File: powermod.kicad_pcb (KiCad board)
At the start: 4 copper layers, 27 x 18 mm, 17 parts, among them J1 Conn_02x07_Odd_Even, J2 Conn_02x07_Odd_Even, U1 TPS54202

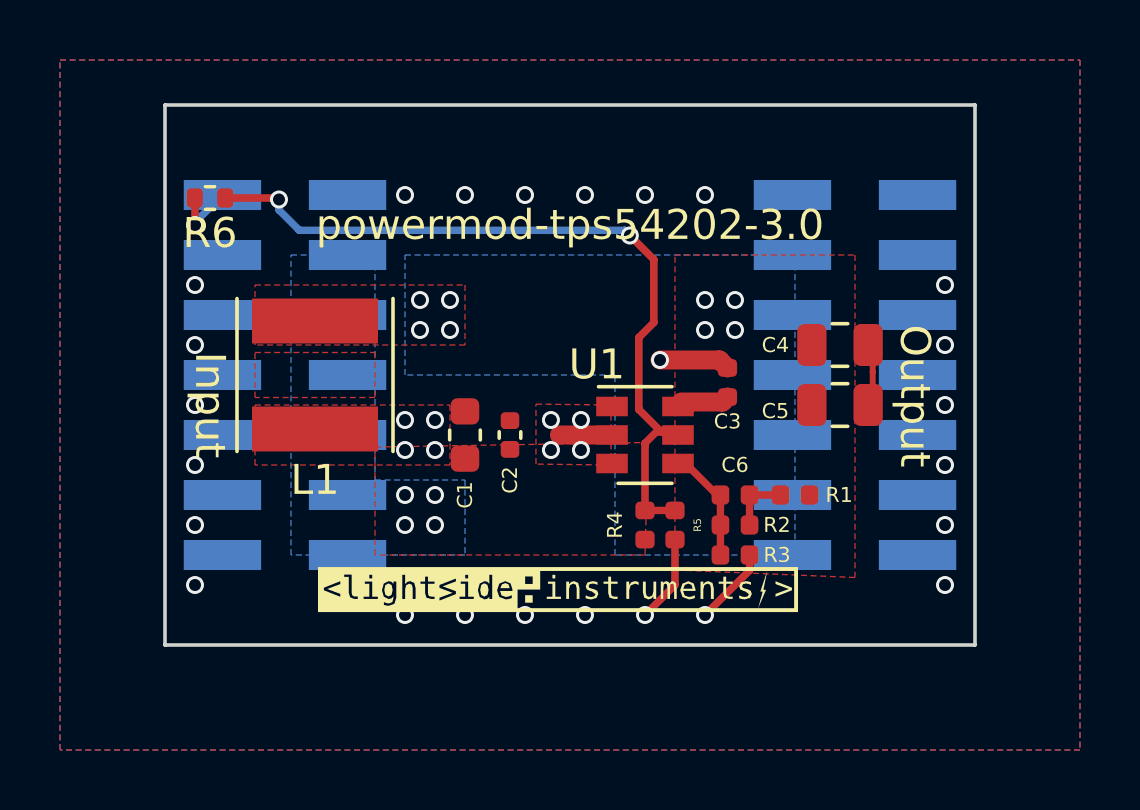
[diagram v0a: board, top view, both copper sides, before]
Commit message: powermod-tps54260
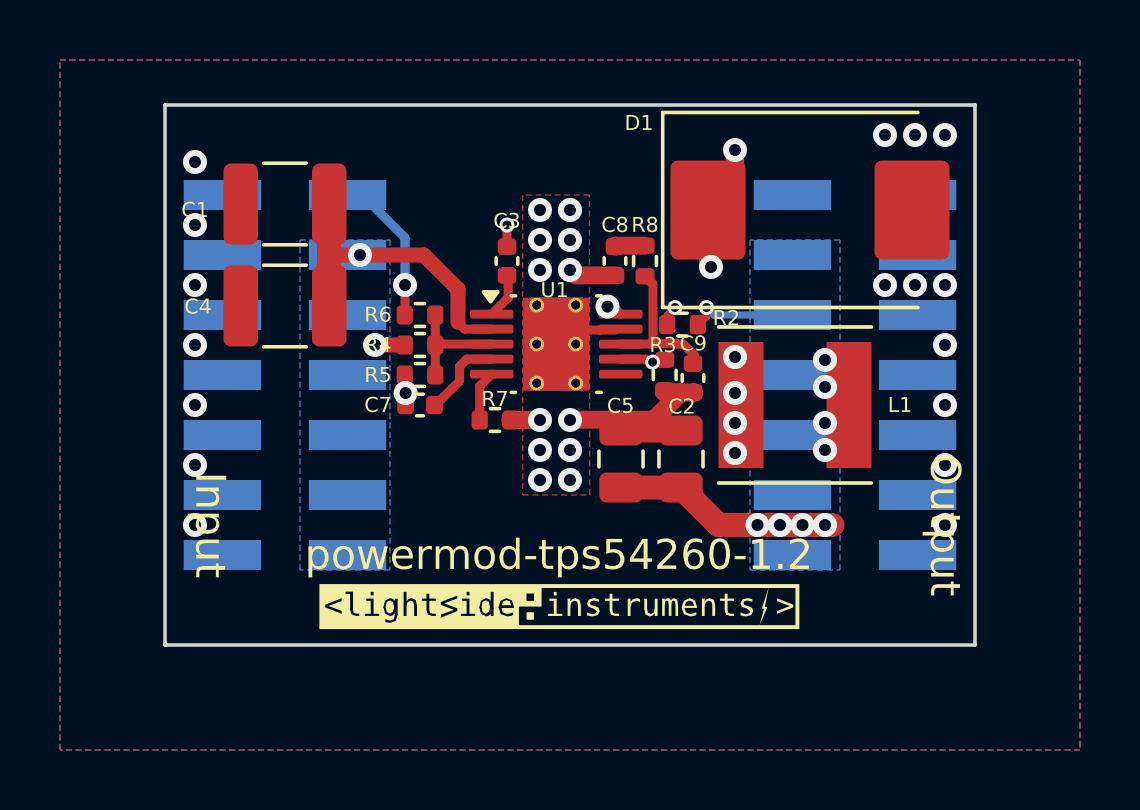
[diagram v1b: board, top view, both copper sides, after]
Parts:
- removed C6: 75 pF, Capacitor_SMD:C_0402_1005Metric
- removed R1: 49.9, Resistor_SMD:R_0402_1005Metric
- added C7: 0.025uF, Capacitor_SMD:C_0402_1005Metric, F.Cu at (24.5, 49.0)
- added C8: 51.1nF, Capacitor_SMD:C_0402_1005Metric, F.Cu at (31.0, 44.2)
- added C9: 14pF, Capacitor_SMD:C_0402_1005Metric, F.Cu at (33.6, 48.1)
- added D1: B360, Diode_SMD:D_SMC, F.Cu at (37.5, 42.5)
- added R7: 240K, Resistor_SMD:R_0402_1005Metric, F.Cu at (27.0, 49.5)
- added R8: 9K, Resistor_SMD:R_0402_1005Metric, F.Cu at (32.0, 44.2)
- C1: value 10uF -> 4.7uF; footprint Capacitor_SMD:C_0603_1608Metric -> Capacitor_SMD:C_1210_3225Metric
- C2: value 0.1uF -> 47uF; footprint Capacitor_SMD:C_0402_1005Metric -> Capacitor_SMD:C_0805_2012Metric
- C4: value 22uF -> 4.7uF; footprint Capacitor_SMD:C_0805_2012Metric -> Capacitor_SMD:C_1210_3225Metric
- C5: value 22uF -> 47uF
- R2: value 100K -> 52K
- R3: value 13.3K -> 11K
- R4: value 511K -> 332K
- R5: value 105K -> 56.2K
- U1: value TPS54202 -> TPS54260DGQ; footprint Package_TO_SOT_SMD:SOT-23-6 -> Package_SO:MSOP-10-1EP_3x3mm_P0.5mm_EP2.2x3.1mm_Mask1.83x1.89mm_ThermalVias
- moved C4 18.5 mm to (20.0, 45.7), turned to 180 degrees
- moved L1 16.0 mm to (37.0, 49.0), turned to 0 degrees
- moved R5 9.86 mm to (24.5, 48.0), turned to 0 degrees
- moved C1 9.76 mm to (20.0, 42.3), turned to 180 degrees
- moved R4 9.60 mm to (24.5, 47.0), turned to 0 degrees
- moved C3 8.39 mm to (27.4, 44.2)
- moved R6 8.01 mm to (24.5, 46.0)
- moved C5 7.52 mm to (31.2, 50.8), turned to 90 degrees
- moved R2 6.91 mm to (33.2, 46.3)
- moved R3 6.44 mm to (32.7, 48.0), turned to -90 degrees
- moved C2 5.76 mm to (33.2, 50.8)
- moved U1 4.24 mm to (29.0, 47.0)
- moved svg2mod 0.57 mm to (29.1, 56.3)
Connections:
- C2 pad 1: SYS_DCIN -> +5V
- C3 pad 2: Net-(C3-Pad2) -> /BOOT
- C4 pad 1: +5V -> SYS_DCIN
- J1 pad 1: unconnected-(J1-Pad1) -> Net-(J1-Pin_1)
- J1 pad 2: Net-(J1-Pad2) -> unconnected-(J1-Pin_2-Pad2)
- R2 pad 1: Net-(C6-Pad1) -> +5V
- R2 pad 2: Net-(C6-Pad2) -> /FB
- R3 pad 1: Net-(C6-Pad2) -> /FB
- R5 pad 1: /ENABLE -> GND
- R5 pad 2: GND -> /ENABLE
- R6 pad 2: Net-(J1-Pad2) -> Net-(J1-Pin_1)
- U1 pad 1: GND -> /BOOT
- U1 pad 2: /SW -> SYS_DCIN
- U1 pad 3: SYS_DCIN -> /ENABLE
- U1 pad 4: Net-(C6-Pad2) -> Net-(U1-SS/TR)
- U1 pad 5: /ENABLE -> Net-(U1-RT/CLK)
- U1 pad 6: Net-(C3-Pad2) -> unconnected-(U1-PWRGD-Pad6)
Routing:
- net /ENABLE: track 27.0 -> 3.91 mm, vias 2 -> 0
- net /SW: track 8.77 -> 22.4 mm, vias 9 -> 8
- net +5V: track 0.00 -> 11.5 mm, vias 8 -> 9
- net SYS_DCIN: track 0.00 -> 11.4 mm, vias 4 -> 2
- net Net-(U1-COMP): track 0.00 -> 5.22 mm
- net Net-(J1-Pin_1): track 0.00 -> 4.60 mm, vias 0 -> 1
- net /FB: track 0.00 -> 3.91 mm, vias 0 -> 2
- net Net-(C6-Pad2): track 3.74 -> 0.00 mm
- net GND: track 7.54 -> 11.2 mm, vias 24 -> 30
- net Net-(U1-SS/TR): track 0.00 -> 2.83 mm
- net Net-(J1-Pad2): track 2.28 -> 0.00 mm, vias 1 -> 0
- net Net-(C6-Pad1): track 2.03 -> 0.00 mm
- net Net-(U1-RT/CLK): track 0.00 -> 1.70 mm
- net Net-(C3-Pad2): track 1.63 -> 0.00 mm
- net /BOOT: track 0.00 -> 1.49 mm
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- added copper zone on In1.Cu, net /SW
- added copper zone on In2.Cu, net GND
- removed copper zone on F.Cu, net (none)
- removed copper zone on F.Cu, net +5V
- removed copper zone on F.Cu, net /SW
- removed copper zone on In2.Cu, net /SW
- removed copper zone on F.Cu, net SYS_DCIN
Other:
- board text added: "Enable pin"
- board text added: "powermod-tps54260-1.2"
- board text removed: "powermod-tps54202-3.0"

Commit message: powermod-tps54260-1.4
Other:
- board text added: "powermod-tps54260-1.4"
- board text removed: "powermod-tps54260-1.2"
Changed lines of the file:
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@@
 		)
 	)
-	(gr_text "powermod-tps54260-1.2"
+	(gr_text "powermod-tps54260-1.4"
 		(at 29.129989 54 0)
 		(layer "F.SilkS")
@@
 	)
 	(segment
+		(start 32.160854 46.838589)
+		(end 32.26686 46.944595)
+		(width 0.2)
+		(layer "F.Cu")
+		(net 14)
+	)
+	(segment
 		(start 33.28 46.97)
 		(end 33.071533 46.97)
@@
 	)
 	(segment
-		(start 32.265 44.975)
-		(end 32.265 46.87186)
-		(width 0.3)
+		(start 32.160854 45.079146)
+		(end 32.160854 46.838589)
+		(width 0.2)
 		(layer "F.Cu")
 		(net 14)
@@
 	)
 	(segment
-		(start 32.265 46.87186)
-		(end 32.229562 46.907298)
-		(width 0.3)
-		(layer "F.Cu")
-		(net 14)
-	)
-	(segment
 		(start 32.26686 46.944595)
 		(end 32.241455 46.97)
@@
 	)
 	(segment
+		(start 32 44.71)
+		(end 32.160854 44.870854)
+		(width 0.3)
+		(layer "F.Cu")
+		(net 14)
+	)
+	(segment
 		(start 33.046128 46.944595)
 		(end 32.26686 46.944595)
@@
 	)
 	(segment
-		(start 32 44.71)
-		(end 32.265 44.975)
-		(width 0.3)
-		(layer "F.Cu")
-		(net 14)
-	)
-	(segment
 		(start 33.635483 47.611462)
 		(end 33.635483 47.325483)
 		(width 0.3)
 		(layer "F.Cu")
+		(net 14)
+	)
+	(segment
+		(start 32.160854 44.870854)
+		(end 32.160854 45.5)
+		(width 0.3)
+		(layer "F.Cu")
